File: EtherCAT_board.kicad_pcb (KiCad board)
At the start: 2 copper layers, 100 x 50 mm, 146 parts, among them J1 CONN_01X12, J10 CONN_01X03, J11 CONN_01X03, J12 CONN_01X03, J13 CONN_01X03, J14 CONN_01X03, J15 CONN_01X03, J16 CONN_01X03, J17 CONN_01X03, J18 CONN_01X03, J19 CONN_01X03, J2 USB_OTG, J20 CONN_01X03, J3 RJ45-PULSETRANS, J4 RJ45-PULSETRANS, J5 CONN_01X03, J6 CONN_01X03, J7 CONN_01X03, J8 CONN_01X03, J9 CONN_01X03, SW1 SKRPACE010, SW2 DIP_SW_8P, SW3 DIP_SW_8P, U1 LAN9252, U2 LM1117-3.3, U3 24LC512, Y1 Crystal_GND24

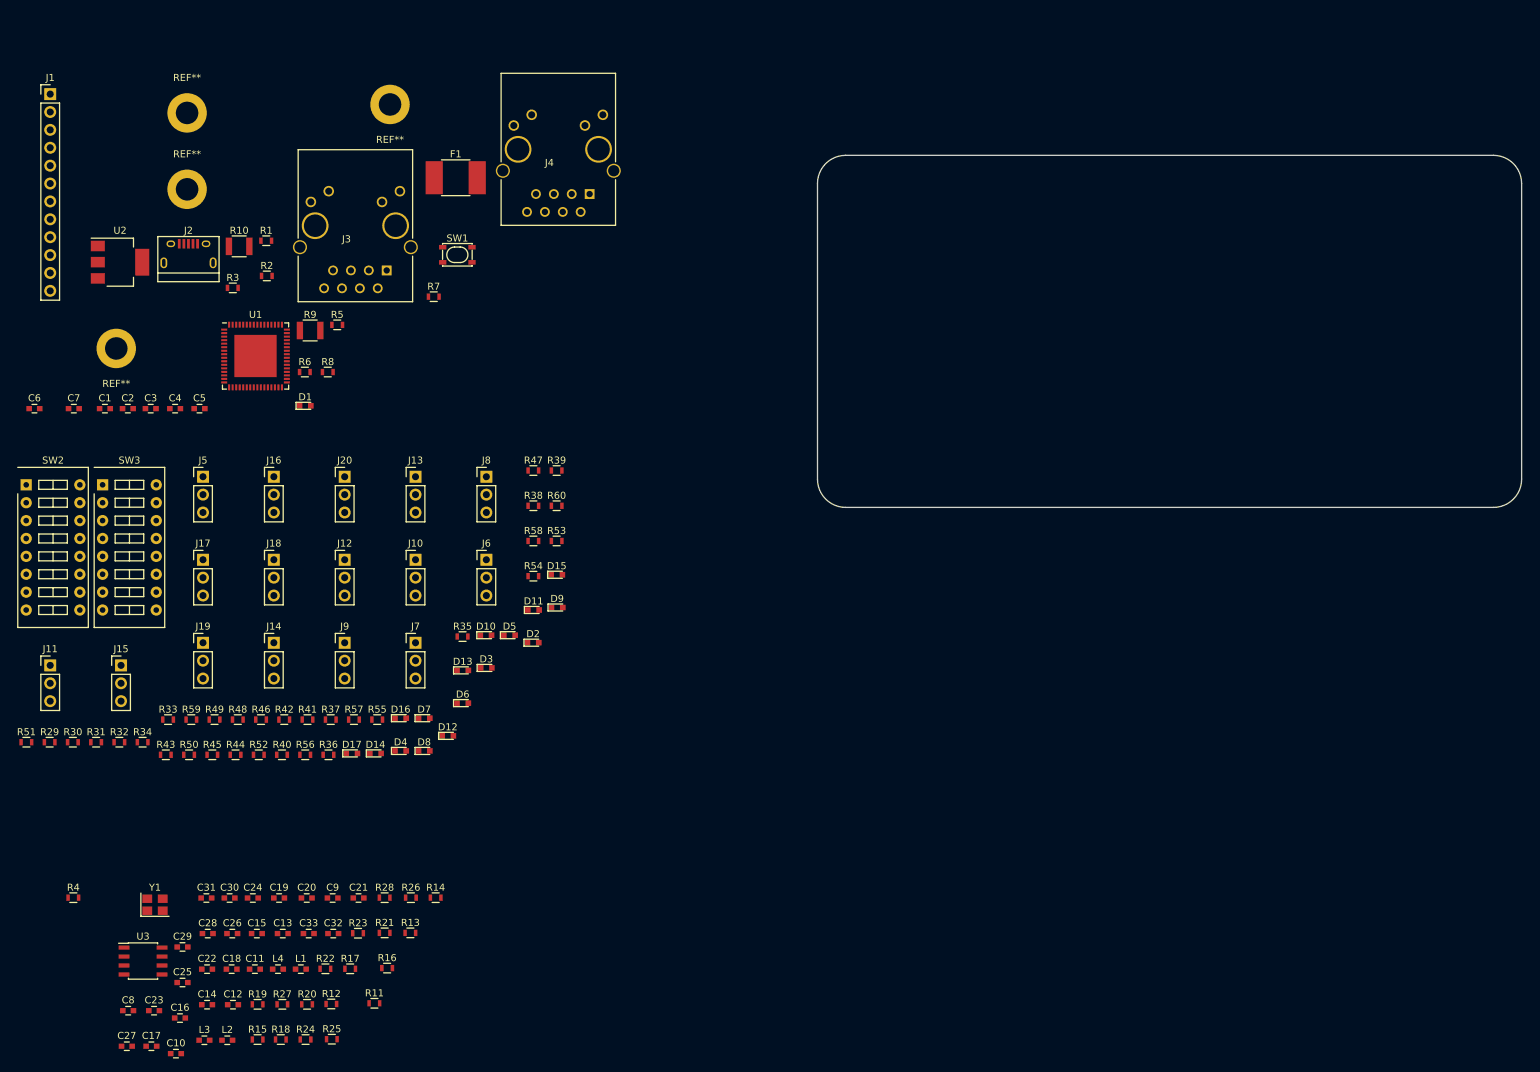
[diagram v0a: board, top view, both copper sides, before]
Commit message: GPIO周りをまとめた
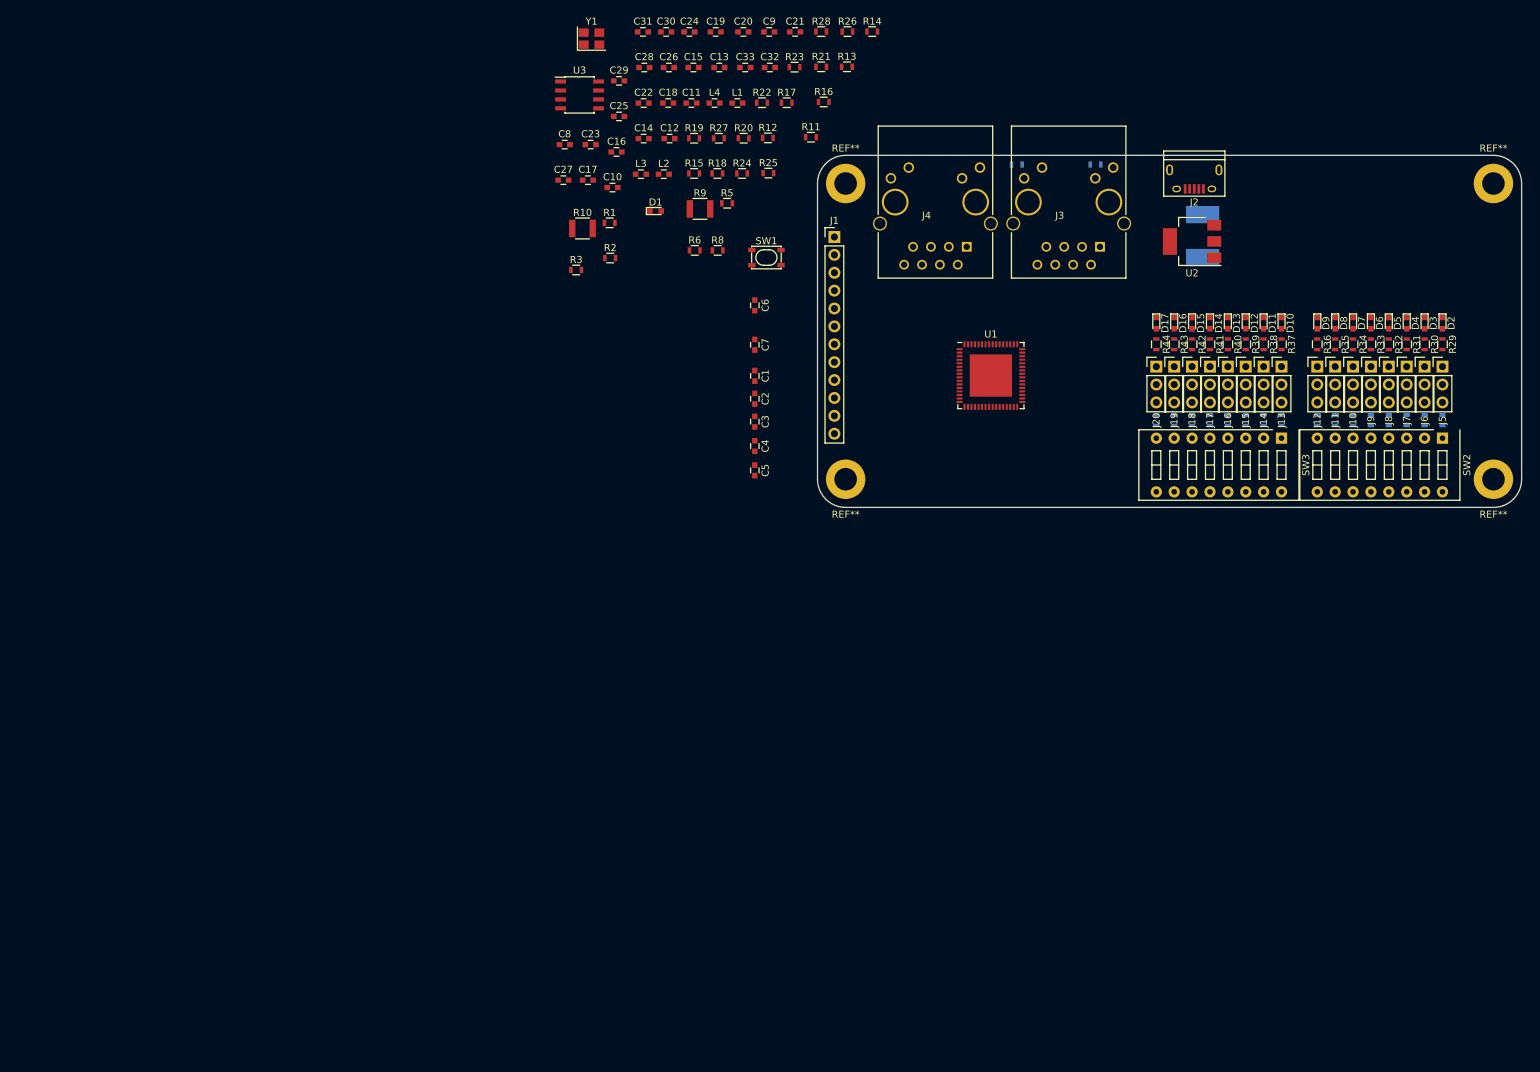
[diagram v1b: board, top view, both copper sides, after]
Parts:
- F1, R4, R45, R46, R47, R48, R49, R50, R51, R52, R53, R54, R55, R56, R57, R58, R59, R60, R7: moved to B.Cu
- moved R29 205.7 mm to (238.8, 76.8), turned to 270 degrees
- moved SW2 201.2 mm to (238.8, 90.2), turned to 270 degrees
- moved R30 200.1 mm to (236.2, 76.8), turned to 270 degrees
- moved R51 198.8 mm to (231.1, 87.6), turned to 90 degrees
- moved REF** 196.5 mm to (246.0, 96.0)
- moved R31 194.5 mm to (233.7, 76.8), turned to 270 degrees
- moved R32 188.9 mm to (231.1, 76.8), turned to 270 degrees
- moved J11 187.4 mm to (223.5, 80.0)
- moved REF** 185.5 mm to (246.0, 54.0)
- moved R45 181.1 mm to (238.8, 87.6), turned to 90 degrees
- moved R34 181.0 mm to (226.1, 76.8), turned to 270 degrees
- moved R33 178.9 mm to (228.6, 76.8), turned to 270 degrees
- moved R4 178.6 mm to (189.5, 51.3), turned to 180 degrees
- moved J5 176.7 mm to (238.8, 80.0)
- moved R49 174.6 mm to (233.7, 87.6), turned to 90 degrees
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
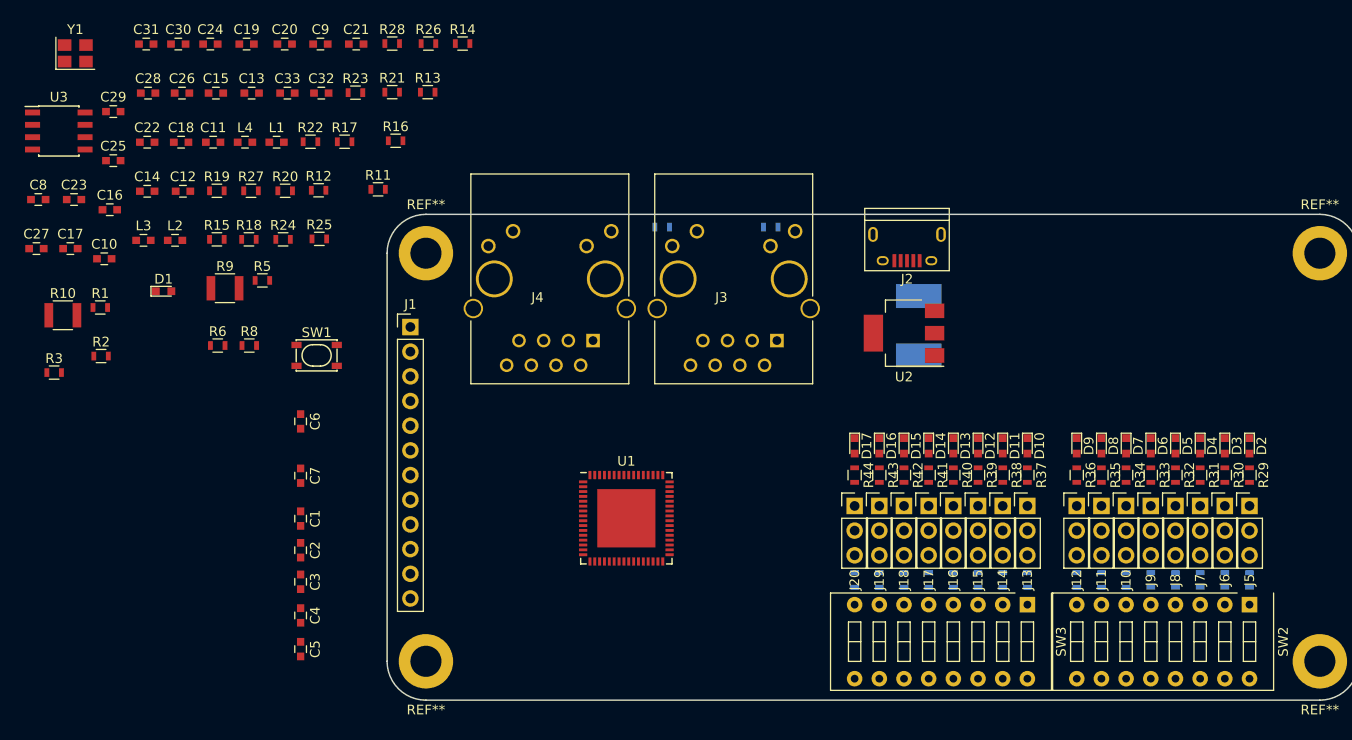
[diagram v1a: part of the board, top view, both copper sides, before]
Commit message: 基板内に部品を納めた
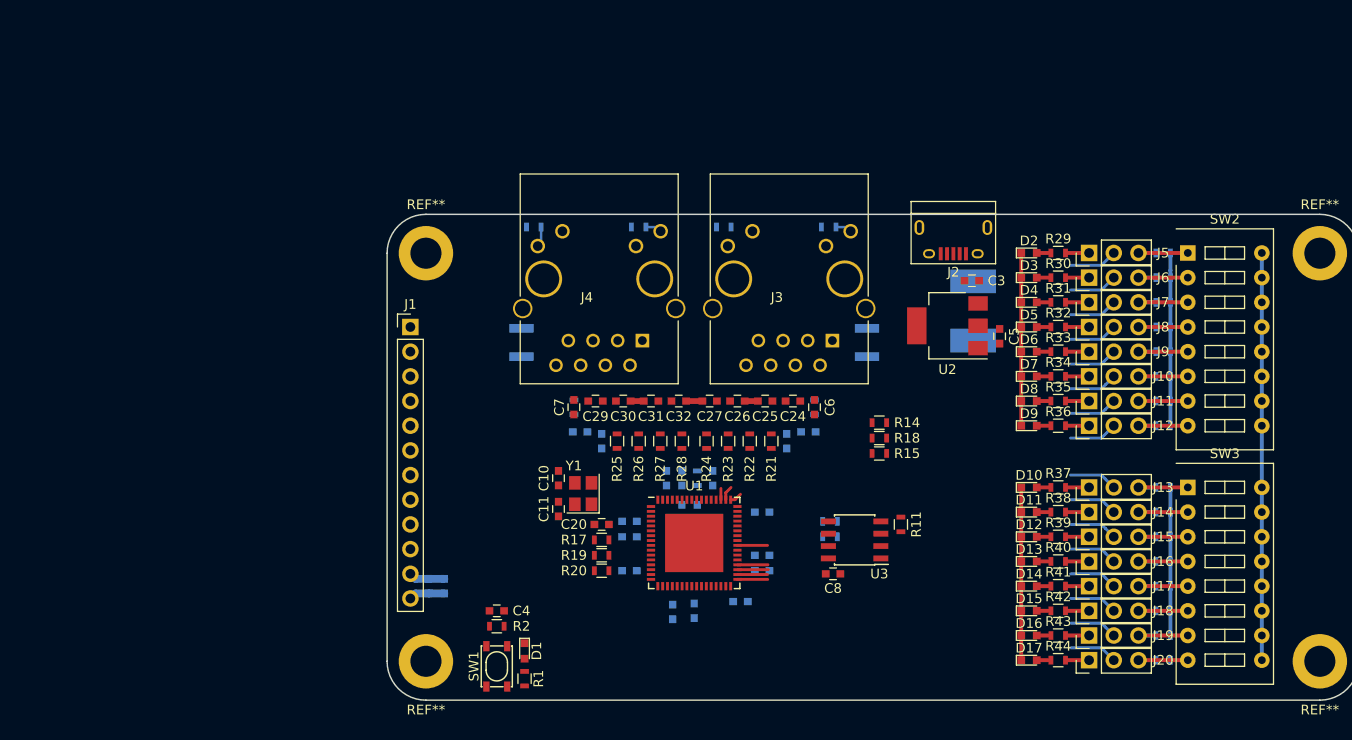
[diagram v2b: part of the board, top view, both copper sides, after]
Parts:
- C1, C12, C13, C14, C15, C16, C17, C18, C19, C2, C21, C22, C23, C28, C33, C9, L1, L2, L3, L4, R10, R12, R13, R16, R3, R5, R6, R8, R9: moved to B.Cu
- moved U3 92.1 mm to (198.1, 83.5), turned to 180 degrees
- moved C8 90.4 mm to (195.9, 87.0), turned to 180 degrees
- moved R10 82.8 mm to (199.4, 63.2), turned to 270 degrees
- moved C5 78.8 mm to (213.0, 62.5)
- moved R3 78.3 mm to (194.0, 69.8), turned to 90 degrees
- moved C22 77.1 mm to (188.6, 86.7)
- moved C28 76.4 mm to (193.4, 72.4)
- moved C3 75.7 mm to (210.2, 56.8), turned to 180 degrees
- moved C19 74.3 mm to (181.6, 90.8), turned to 90 degrees
- moved C16 74.0 mm to (188.6, 80.6), turned to 180 degrees
- moved C18 73.4 mm to (188.6, 85.1)
- moved C9 71.8 mm to (186.4, 89.9), turned to 180 degrees
- moved C23 71.8 mm to (181.9, 80.6), turned to 90 degrees
- moved R15 71.7 mm to (200.7, 74.6)
- moved C25 71.5 mm to (188.9, 69.2), turned to 180 degrees
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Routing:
- net GND: track 0.00 -> 85.6 mm
- net +3V3: track 0.00 -> 36.7 mm
- net GPIO0: track 0.00 -> 8.11 mm
- net GPIO9: track 0.00 -> 8.08 mm
- net GPIO2: track 0.00 -> 8.07 mm
- net IN_DGIO9: track 0.00 -> 6.87 mm
- net IN_DGIO8: track 0.00 -> 6.87 mm
- net IN_DGIO7: track 0.00 -> 6.87 mm
- net IN_DGIO6: track 0.00 -> 6.87 mm
- net IN_DGIO5: track 0.00 -> 6.87 mm
- net IN_DGIO4: track 0.00 -> 6.87 mm
- net IN_DGIO3: track 0.00 -> 6.87 mm
- net IN_DGIO2: track 0.00 -> 6.87 mm
- net IN_DGIO14: track 0.00 -> 6.87 mm
- net IN_DGIO13: track 0.00 -> 6.87 mm
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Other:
- net class Default: clearance 0.2 -> 0.199
- rule trace_clearance: 0.2 -> 0.199

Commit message: GPIOまわりを配線
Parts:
- moved C12 5.64 mm to (174.0, 89.2)
- moved C19 5.64 mm to (176.6, 93.3)
- moved R6 5.12 mm to (181.0, 51.0), turned to 0 degrees
- moved R7 4.99 mm to (189.4, 52.8), turned to 90 degrees
- moved R11 4.48 mm to (204.7, 77.8)
- moved C8 4.48 mm to (197.7, 82.9)
- moved R13 4.48 mm to (197.4, 79.1)
- moved R12 4.48 mm to (197.4, 77.5)
- moved U3 4.48 mm to (199.9, 79.4)
- moved R15 4.25 mm to (197.4, 71.9), turned to 90 degrees
- moved R4 3.99 mm to (199.4, 51.8), turned to 270 degrees
- moved C11 3.45 mm to (168.9, 77.1)
- moved Y1 3.27 mm to (171.4, 75.7)
- moved C10 3.20 mm to (168.9, 74.2)
- moved C9 3.08 mm to (186.9, 86.8)
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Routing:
- net GND: track 85.6 -> 163.0 mm, vias 0 -> 25
- net GPIO14: track 4.97 -> 52.6 mm, vias 0 -> 1
- net GPIO13: track 4.97 -> 49.0 mm, vias 0 -> 1
- net GPIO15: track 4.97 -> 48.1 mm, vias 0 -> 1
- net GPIO11: track 4.97 -> 47.9 mm, vias 0 -> 1
- net GPIO12: track 4.97 -> 47.5 mm, vias 0 -> 1
- net GPIO10: track 4.97 -> 45.8 mm, vias 0 -> 1
- net GPIO9: track 8.08 -> 43.7 mm, vias 0 -> 1
- net +3V3: track 36.7 -> 60.9 mm, vias 0 -> 2
- net /LAN9252/VDD33TXRX2: track 0.00 -> 23.9 mm, vias 0 -> 3
- net /LAN9252/VDD33TXRX1: track 1.16 -> 24.9 mm, vias 0 -> 3
- net /LAN9252/RUNLED: track 0.00 -> 20.6 mm, vias 0 -> 1
- net /TX1_N: track 0.00 -> 14.0 mm
- net /TX1_P: track 0.00 -> 14.0 mm
- net /TX2_P: track 0.00 -> 13.2 mm
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
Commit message: 5Vの電源LEDを追加 ポリスイッチのサイズを3225に変更
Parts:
- added D18: LED, LEDs:LED_0603, F.Cu at (204.7, 59.8)
- added R61: 1k, Resistors_SMD:R_0603, F.Cu at (204.7, 61.3)
- C8, R11, R19, R20, U3: moved to B.Cu
- F1: footprint Resistors_SMD:R_2816 -> Resistors_SMD:R_1210; moved to F.Cu
- moved C13 14.6 mm to (189.3, 83.7), turned to 180 degrees
- moved C18 13.8 mm to (175.0, 80.6), turned to 180 degrees
- moved C5 12.9 mm to (205.6, 73.1), turned to 180 degrees
- moved C19 9.10 mm to (182.3, 86.3)
- moved C3 8.11 mm to (204.7, 62.8)
- moved C8 7.37 mm to (197.7, 75.5)
- moved C12 6.60 mm to (179.9, 86.3)
- moved U2 6.55 mm to (207.8, 68.0), turned to 270 degrees
- moved R12 3.54 mm to (193.9, 77.9), turned to 270 degrees
- moved R11 2.46 mm to (204.5, 80.3), turned to 270 degrees
- moved R13 2.36 mm to (195.4, 77.9), turned to 270 degrees
- moved C22 2.26 mm to (189.3, 82.1)
- moved F1 2.21 mm to (208.1, 59.8)
- moved C16 0.70 mm to (189.3, 78.0)
- moved U3 0.39 mm to (199.9, 79.0)
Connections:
- J2 pad 2: (no net) -> Net-(J2-Pad2)
- J2 pad 3: (no net) -> Net-(J2-Pad3)
- J2 pad 4: (no net) -> Net-(J2-Pad4)
- SW1 pad 1: (no net) -> Net-(SW1-Pad1)
- SW1 pad 3: (no net) -> Net-(SW1-Pad3)
- U1 pad 25: (no net) -> Net-(U1-Pad25)
- U1 pad 3: (no net) -> Net-(U1-Pad3)
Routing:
- net GPIO8: track 0.00 -> 76.0 mm, vias 0 -> 1
- net LATCH0: track 0.00 -> 64.7 mm, vias 0 -> 1
- net GPIO4: track 4.97 -> 69.3 mm, vias 0 -> 3
- net GPIO7: track 4.97 -> 67.0 mm, vias 0 -> 3
- net GPIO5: track 11.6 -> 68.3 mm, vias 0 -> 3
- net GPIO6: track 11.9 -> 67.8 mm, vias 0 -> 3
- net GPIO0: track 4.97 -> 60.1 mm, vias 0 -> 1
- net GPIO1: track 4.97 -> 58.4 mm, vias 0 -> 1
- net +3V3: track 60.9 -> 110.4 mm, vias 2 -> 5
- net SIO3: track 0.00 -> 45.8 mm
- net GND: track 163.0 -> 207.2 mm, vias 25 -> 37
- net GPIO3: track 4.97 -> 36.8 mm, vias 0 -> 1
- net SI/SIO0: track 1.15 -> 32.1 mm
- net SO/SIO1: track 0.00 -> 26.5 mm, vias 0 -> 1
- net SIO2: track 0.00 -> 25.9 mm, vias 0 -> 2
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- added copper zone on F.Cu, net +5V
- added copper zone on B.Cu, net GND
- added copper zone on F.Cu, net GND

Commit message: 進捗
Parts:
- C14, R19, R20: moved to F.Cu
- C20, R17: moved to B.Cu
- moved C20 5.83 mm to (177.9, 79.4), turned to 90 degrees
- moved R17 3.88 mm to (175.9, 81.8), turned to 180 degrees
- moved R20 3.82 mm to (170.5, 80.8), turned to 270 degrees
- moved C18 1.93 mm to (176.5, 79.4), turned to 90 degrees
- moved R19 1.88 mm to (172.0, 80.8), turned to 90 degrees
- moved C14 1.32 mm to (174.2, 80.3)
- moved C15 1.10 mm to (175.9, 83.7), turned to 180 degrees
- moved C11 0.85 mm to (168.6, 77.9)
- moved C10 0.76 mm to (168.6, 74.9)
- moved Y1 0.76 mm to (171.1, 76.4)
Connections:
- J1 pad 1: LATCH0 -> SIO3
- J1 pad 10: SIO3 -> RESET
- J1 pad 2: LATCH1 -> SIO2
- J1 pad 3: IRQ -> SO/SIO1
- J1 pad 4: RESET -> SI/SIO0
- J1 pad 7: SI/SIO0 -> LATCH1
- J1 pad 8: SO/SIO1 -> LATCH0
- J1 pad 9: SIO2 -> IRQ
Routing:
- net ~SCS: track 3.96 -> 72.9 mm, vias 1 -> 3
- net GND: track 207.2 -> 267.3 mm, vias 37 -> 47
- net IRQ: track 9.18 -> 57.4 mm, vias 1 -> 2
- net SCK: track 4.88 -> 36.3 mm, vias 0 -> 1
- net Net-(C18-Pad1): track 4.18 -> 35.2 mm, vias 2 -> 3
- net LATCH1: track 4.11 -> 31.4 mm
- net +3V3: track 110.4 -> 132.8 mm, vias 5 -> 9
- net RESET: track 0.00 -> 21.8 mm
- net SIO3: track 45.8 -> 65.2 mm, vias 0 -> 1
- net LATCH0: track 64.7 -> 46.2 mm, vias 1 -> 0
- net SIO2: track 25.9 -> 37.8 mm, vias 2 -> 0
- net Net-(C11-Pad1): track 0.00 -> 11.5 mm
- net Net-(C10-Pad2): track 0.00 -> 10.6 mm
- net SO/SIO1: track 26.5 -> 35.9 mm, vias 1 -> 0
- net Net-(R20-Pad2): track 0.00 -> 6.95 mm
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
